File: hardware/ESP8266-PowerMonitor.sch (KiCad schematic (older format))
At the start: 19 parts, among them J1 CONN_PULSE, J2 CONN_PROG, J3 CONN_AC, J4 CONN_TEMP, SW1 SW_RESET, U1 AMS1117-3.3, U2 ESP-12F

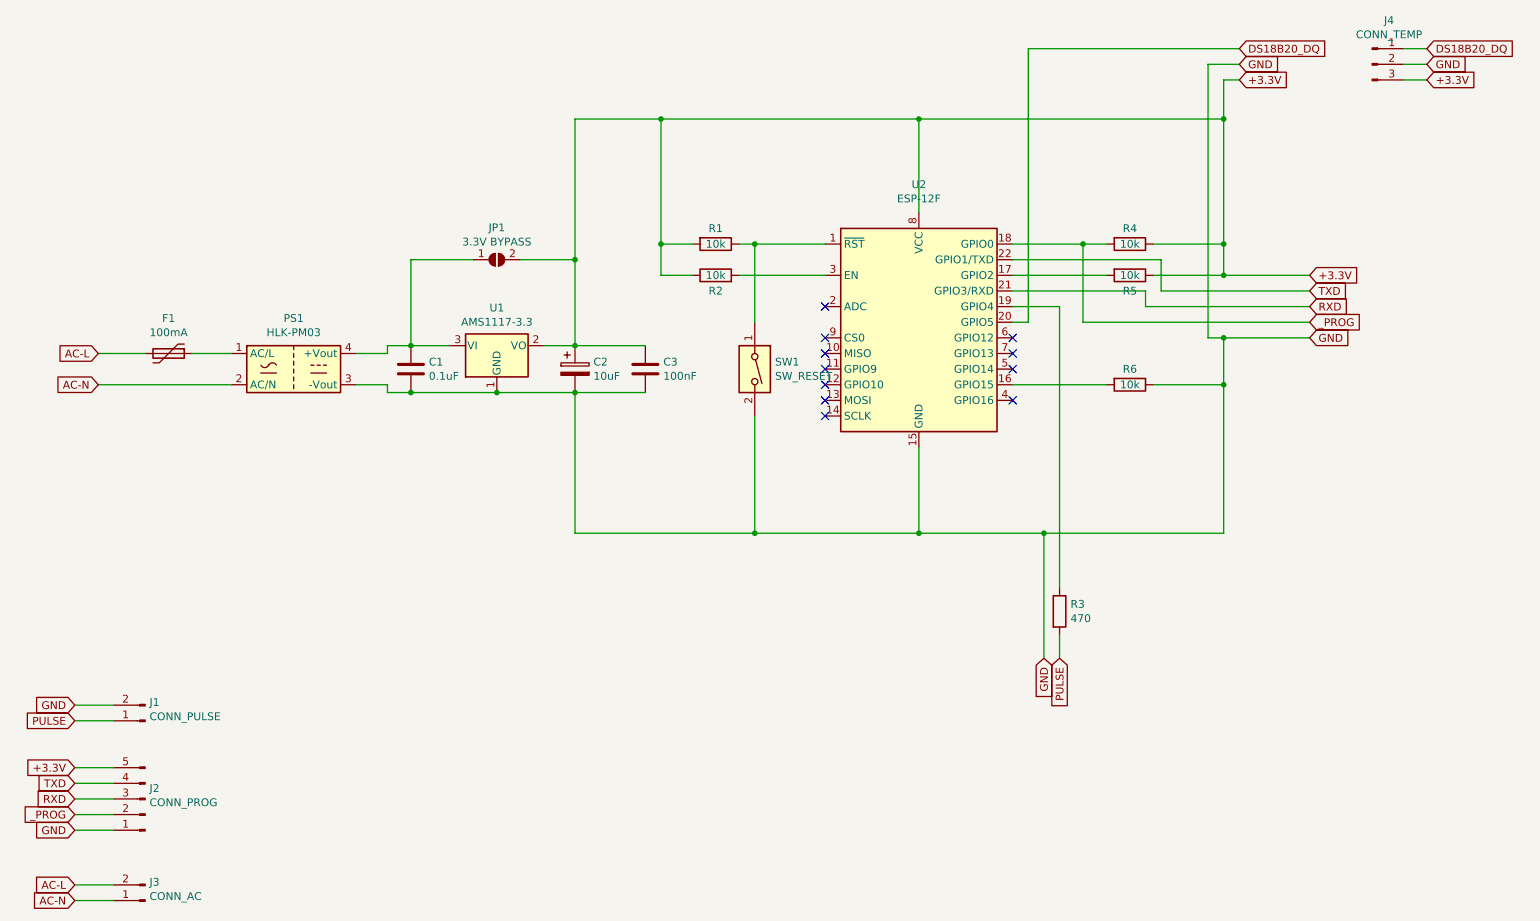
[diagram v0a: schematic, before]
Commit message: * Reworked the board to use 0.5/1.3mm vias. * Added I2C to GPIO4/5 in case we want to use an OLED display. * Moved the pulse pin to GPIO2 (pulled up). * Re-orged the board to use fewer vias.
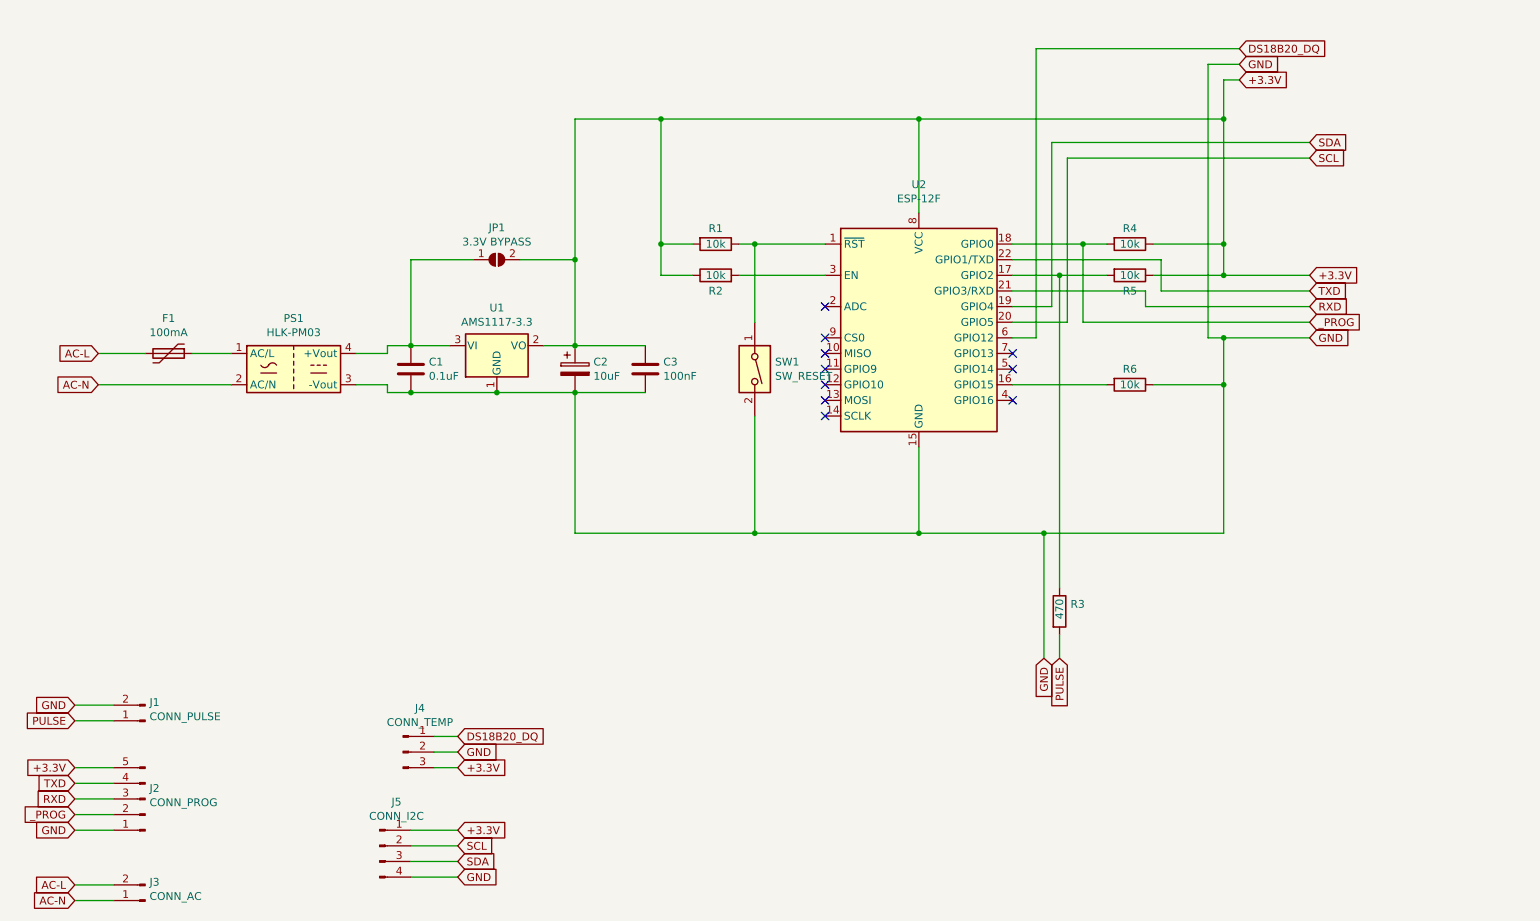
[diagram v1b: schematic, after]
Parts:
- added J5: CONN_I2C, Connector_PinHeader_2.54mm:PinHeader_1x04_P2.54mm_Vertical, symbol Connector:Conn_01x04_Male
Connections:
- net +3.3V: now also J5.1 (Pin_1)
- net DS18B20_DQ: now also U2.6 (GPIO12); no longer U2.20 (GPIO5)
- net GND: now also J5.4 (Pin_4)
- net at R5.2, U2.17 (GPIO2): now also R3.1
- net SDA: now reaches U2.19 (GPIO4)
- net SDA: now also J5.3 (Pin_3); no longer R3.1
- new net SCL: J5.2 (Pin_2), U2.20 (GPIO5)
- no-connect marks 11 -> 10
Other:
- moved on the sheet: J4
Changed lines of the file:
@@
 $EndComp
 Wire Wire Line
-	7450 3250 8050 3250
+	7450 3250 7750 3250
 Wire Wire Line
 	8350 3250 8800 3250
@@
 P 7750 5400
 F 0 "R3" H 7820 5446 50  0000 L CNN
-F 1 "470" H 7820 5355 50  0000 L CNN
+F 1 "470" V 7750 5350 50  0000 L CNN
 F 2 "Resistor_SMD:R_1206_3216Metric_Pad1.42x1.75mm_HandSolder" V 7680 5400 50  0001 C CNN
 F 3 "~" H 7750 5400 50  0001 C CNN
@@
 	7750 5550 7750 5700
 Wire Wire Line
-	7750 5250 7750 3450
-Wire Wire Line
-	7750 3450 7450 3450
-Wire Wire Line
 	7650 5700 7650 4900
 Connection ~ 7650 4900
 Wire Wire Line
 	7650 4900 8800 4900
-Wire Wire Line
-	7450 3550 7550 3550
 $Comp
 L Converter_ACDC:HLK-PM03 PS1
@@
 	3450 4000 3600 4000
 Connection ~ 3600 4000
-Wire Wire Line
-	7550 1800 7550 3550
 $Comp
 L Device:C C3
@@
 NoConn ~ 7450 4050
 NoConn ~ 7450 3850
-NoConn ~ 7450 3750
-NoConn ~ 7450 3650
 Wire Wire Line
 	1700 7250 1450 7250
@@
 	8700 3650 8800 3650
 Connection ~ 8800 3650
-Wire Wire Line
-	7550 1800 8900 1800
-Text GLabel 10100 1800 2    50   Input ~ 0
+Text GLabel 3900 6200 2    50   Input ~ 0
 DS18B20_DQ
-Text GLabel 10100 1900 2    50   Input ~ 0
-GND
-Text GLabel 10100 2000 2    50   Input ~ 0
+Text GLabel 3900 6300 2    50   Input ~ 0
+GND
+Text GLabel 3900 6400 2    50   Input ~ 0
 +3.3V
 $Comp
 L Connector:Conn_01x03_Male J4
 U 1 1 5EA4E231
-P 9750 1900
-F 0 "J4" H 9858 2181 50  0000 C CNN
-F 1 "CONN_TEMP" H 9858 2090 50  0000 C CNN
-F 2 "Connector_PinHeader_2.54mm:PinHeader_1x03_P2.54mm_Vertical" H 9750 1900 50  0001 C CNN
-F 3 "~" H 9750 1900 50  0001 C CNN
-	1    9750 1900
-	1    0    0    -1
-$EndComp
-Wire Wire Line
-	10100 1800 9950 1800
-Wire Wire Line
-	9950 1900 10100 1900
-Wire Wire Line
-	10100 2000 9950 2000
+P 3550 6300
+F 0 "J4" H 3658 6581 50  0000 C CNN
+F 1 "CONN_TEMP" H 3658 6490 50  0000 C CNN
+F 2 "Connector_PinHeader_2.54mm:PinHeader_1x03_P2.54mm_Vertical" H 3550 6300 50  0001 C CNN
+F 3 "~" H 3550 6300 50  0001 C CNN
+	1    3550 6300
+	1    0    0    -1
+$EndComp
+Wire Wire Line
+	3900 6200 3750 6200
+Wire Wire Line
+	3750 6300 3900 6300
+Wire Wire Line
+	3900 6400 3750 6400
+Text GLabel 9350 2400 2    50   Input ~ 0
+SDA
+Text GLabel 9350 2500 2    50   Input ~ 0
+SCL
+Wire Wire Line
+	9350 2500 7800 2500
+Wire Wire Line
+	7800 2500 7800 3550
+Wire Wire Line
+	7800 3550 7450 3550
+Wire Wire Line
+	9350 2400 7700 2400
+Wire Wire Line
+	7700 2400 7700 3450
+Wire Wire Line
+	7700 3450 7450 3450
+Wire Wire Line
+	7600 3650 7600 1800
+Wire Wire Line
+	7600 1800 8900 1800
+Wire Wire Line
+	7600 3650 7450 3650
+Text GLabel 3900 6800 2    50   Input ~ 0
++3.3V
+Text GLabel 3900 7000 2    50   Input ~ 0
+SDA
+Text GLabel 3900 6900 2    50   Input ~ 0
+SCL
+Text GLabel 3900 7100 2    50   Input ~ 0
+GND
+$Comp
+L Connector:Conn_01x04_Male J5
+U 1 1 5EAA8055
+P 3400 6900
+F 0 "J5" H 3508 7181 50  0000 C CNN
+F 1 "CONN_I2C" H 3508 7090 50  0000 C CNN
+F 2 "Connector_PinHeader_2.54mm:PinHeader_1x04_P2.54mm_Vertical" H 3400 6900 50  0001 C CNN
+F 3 "~" H 3400 6900 50  0001 C CNN
+	1    3400 6900
+	1    0    0    -1
+$EndComp
+Wire Wire Line
+	3600 6800 3900 6800
+Wire Wire Line
+	3900 7100 3600 7100
+Wire Wire Line
+	7750 5250 7750 3250
+Connection ~ 7750 3250
+Wire Wire Line
+	7750 3250 8050 3250
+NoConn ~ 7450 3750
+Wire Wire Line
+	3900 6900 3600 6900
+Wire Wire Line
+	3600 7000 3900 7000
 $EndSCHEMATC

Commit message: Updated PCB, uses GPIO13 instead of GPIO2, which didn't work.
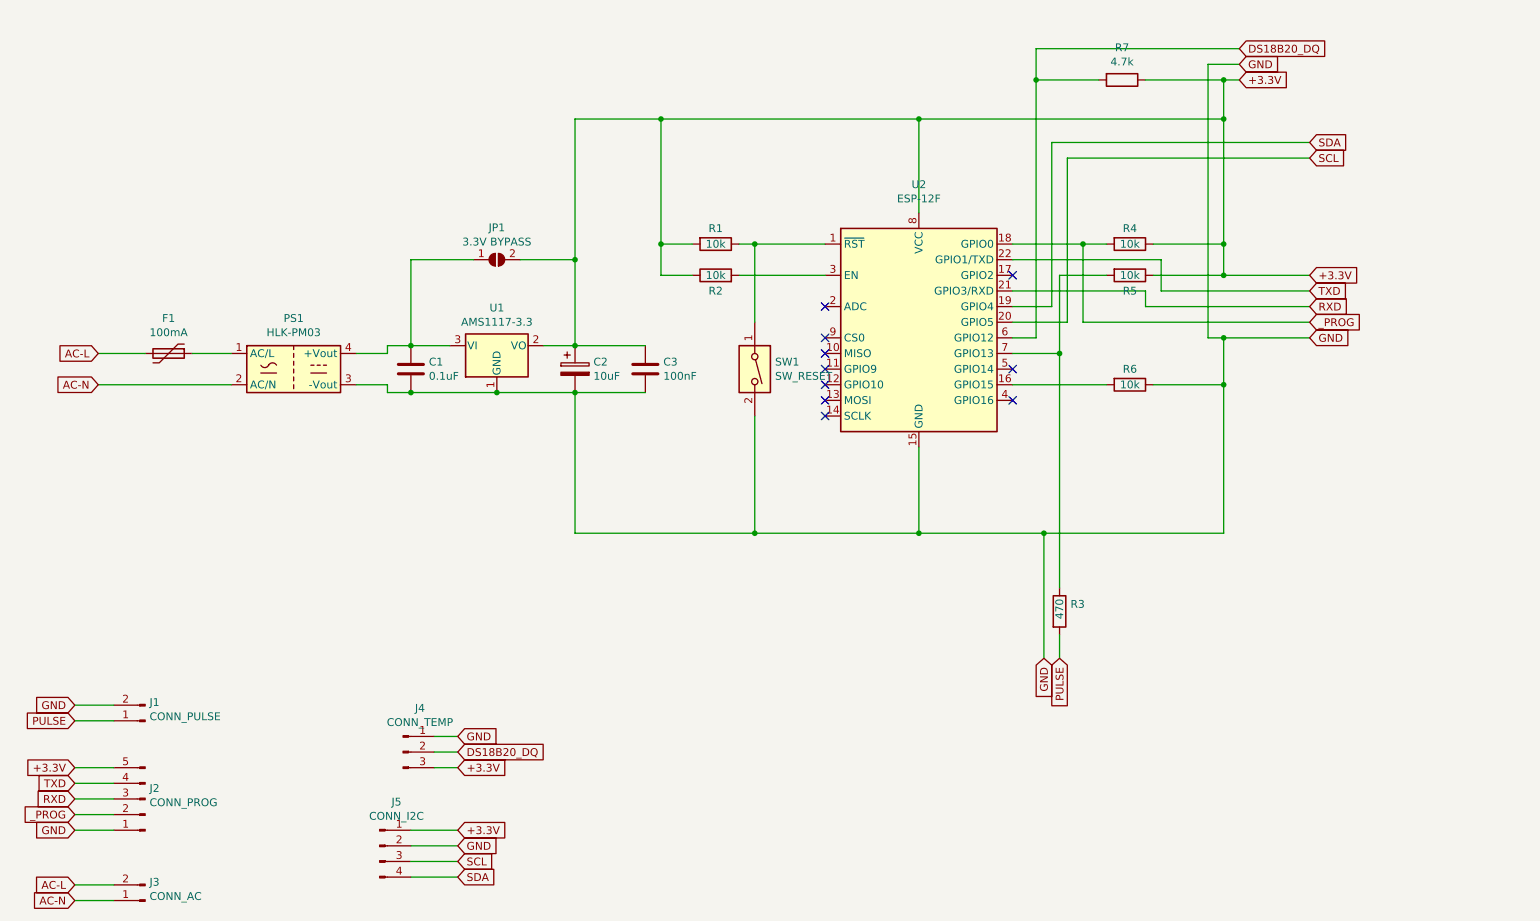
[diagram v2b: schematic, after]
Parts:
- added R7: 4.7k, Resistor_SMD:R_1206_3216Metric_Pad1.42x1.75mm_HandSolder, symbol Device:R
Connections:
- net +3.3V: now also R7.1
- net DS18B20_DQ: now also J4.2 (Pin_2), R7.2; no longer J4.1 (Pin_1)
- net GND: now also J4.1 (Pin_1), J5.2 (Pin_2); no longer J4.2 (Pin_2), J5.4 (Pin_4)
- net SCL: now also J5.3 (Pin_3); no longer J5.2 (Pin_2)
- net SDA: now also J5.4 (Pin_4); no longer J5.3 (Pin_3)
- net at R3.1, R5.2: now also U2.7 (GPIO13); no longer U2.17 (GPIO2)
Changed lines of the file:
@@
 	0    1    1    0
 $EndComp
-Wire Wire Line
-	7450 3250 7750 3250
-Wire Wire Line
-	8350 3250 8800 3250
-Connection ~ 8800 3250
 $Comp
 L Device:R R3
@@
 	8700 3650 8800 3650
 Connection ~ 8800 3650
+Text GLabel 3900 6300 2    50   Input ~ 0
+DS18B20_DQ
 Text GLabel 3900 6200 2    50   Input ~ 0
-DS18B20_DQ
-Text GLabel 3900 6300 2    50   Input ~ 0
 GND
 Text GLabel 3900 6400 2    50   Input ~ 0
@@
 	1    0    0    -1
 $EndComp
-Wire Wire Line
-	3900 6200 3750 6200
-Wire Wire Line
-	3750 6300 3900 6300
-Wire Wire Line
-	3900 6400 3750 6400
 Text GLabel 9350 2400 2    50   Input ~ 0
 SDA
@@
 	7700 3450 7450 3450
 Wire Wire Line
-	7600 3650 7600 1800
+	7600 3650 7600 2000
 Wire Wire Line
 	7600 1800 8900 1800
@@
 Text GLabel 3900 6800 2    50   Input ~ 0
 +3.3V
+Text GLabel 3900 7100 2    50   Input ~ 0
+SDA
 Text GLabel 3900 7000 2    50   Input ~ 0
-SDA
+SCL
 Text GLabel 3900 6900 2    50   Input ~ 0
-SCL
-Text GLabel 3900 7100 2    50   Input ~ 0
 GND
 $Comp
@@
 	3600 6800 3900 6800
 Wire Wire Line
-	3900 7100 3600 7100
-Wire Wire Line
-	7750 5250 7750 3250
-Connection ~ 7750 3250
-Wire Wire Line
-	7750 3250 8050 3250
-NoConn ~ 7450 3750
-Wire Wire Line
-	3900 6900 3600 6900
-Wire Wire Line
-	3600 7000 3900 7000
+	8800 3250 8350 3250
+Connection ~ 8800 3250
+Wire Wire Line
+	7750 5250 7750 3750
+Wire Wire Line
+	7750 3750 7450 3750
+Wire Wire Line
+	8050 3250 7750 3250
+Wire Wire Line
+	7750 3250 7750 3750
+Connection ~ 7750 3750
+Wire Wire Line
+	3900 6200 3750 6200
+Wire Wire Line
+	3750 6300 3900 6300
+Wire Wire Line
+	3900 6400 3750 6400
+Wire Wire Line
+	3600 6900 3900 6900
+Wire Wire Line
+	3900 7000 3600 7000
+Wire Wire Line
+	3600 7100 3900 7100
+$Comp
+L Device:R R7
+U 1 1 5ECB0601
+P 8150 2000
+F 0 "R7" V 7943 2000 50  0000 C CNN
+F 1 "4.7k" V 8034 2000 50  0000 C CNN
+F 2 "Resistor_SMD:R_1206_3216Metric_Pad1.42x1.75mm_HandSolder" V 8080 2000 50  0001 C CNN
+F 3 "~" H 8150 2000 50  0001 C CNN
+	1    8150 2000
+	0    1    1    0
+$EndComp
+Wire Wire Line
+	8300 2000 8800 2000
+Connection ~ 8800 2000
+Wire Wire Line
+	8000 2000 7600 2000
+Connection ~ 7600 2000
+Wire Wire Line
+	7600 2000 7600 1800
+NoConn ~ 7450 3250
 $EndSCHEMATC
